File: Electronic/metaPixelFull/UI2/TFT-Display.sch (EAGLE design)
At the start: 34 parts, among them IC1 74HCT14N, IC2 74HCT14N, IC3 74HCT74N, Q1 2N3906

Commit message: minor changes
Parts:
- U$1: value 2.2_TFT_LCD -> 2.2_TFT_LCDNEW; device 2.2"tft:2.2_TFT_LCD -> 2.2"tft:2.2_TFT_LCDNEW
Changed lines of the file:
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@@
 <grid distance="0.1" unitdist="inch" unit="inch" style="lines" multiple="1" display="no" altdistance="0.01" altunitdist="inch" altunit="inch"/>
 <layers>
-<layer number="1" name="Top" color="4" fill="1" visible="no" active="no"/>
-<layer number="2" name="Route2" color="1" fill="3" visible="no" active="no"/>
-<layer number="3" name="Route3" color="4" fill="3" visible="no" active="no"/>
-<layer number="14" name="Route14" color="1" fill="6" visible="no" active="no"/>
-<layer number="15" name="Route15" color="4" fill="6" visible="no" active="no"/>
-<layer number="16" name="Bottom" color="1" fill="1" visible="no" active="no"/>
-<layer number="17" name="Pads" color="2" fill="1" visible="no" active="no"/>
-<layer number="18" name="Vias" color="2" fill="1" visible="no" active="no"/>
-<layer number="19" name="Unrouted" color="6" fill="1" visible="no" active="no"/>
-<layer number="20" name="Dimension" color="15" fill="1" visible="no" active="no"/>
-<layer number="21" name="tPlace" color="7" fill="1" visible="no" active="no"/>
-<layer number="22" name="bPlace" color="7" fill="1" visible="no" active="no"/>
-<layer number="23" name="tOrigins" color="15" fill="1" visible="no" active="no"/>
-<layer number="24" name="bOrigins" color="15" fill="1" visible="no" active="no"/>
-<layer number="25" name="tNames" color="7" fill="1" visible="no" active="no"/>
-<layer number="26" name="bNames" color="7" fill="1" visible="no" active="no"/>
-<layer number="27" name="tValues" color="7" fill="1" visible="no" active="no"/>
-<layer number="28" name="bValues" color="7" fill="1" visible="no" active="no"/>
+<layer number="1" name="Top" color="4" fill="1" visible="yes" active="no"/>
+<layer number="2" name="Route2" color="1" fill="3" visible="yes" active="no"/>
+<layer number="3" name="Route3" color="4" fill="3" visible="yes" active="no"/>
+<layer number="14" name="Route14" color="1" fill="6" visible="yes" active="no"/>
+<layer number="15" name="Route15" color="4" fill="6" visible="yes" active="no"/>
+<layer number="16" name="Bottom" color="1" fill="1" visible="yes" active="no"/>
+<layer number="17" name="Pads" color="2" fill="1" visible="yes" active="no"/>
+<layer number="18" name="Vias" color="2" fill="1" visible="yes" active="no"/>
+<layer number="19" name="Unrouted" color="6" fill="1" visible="yes" active="no"/>
+<layer number="20" name="Dimension" color="15" fill="1" visible="yes" active="no"/>
+<layer number="21" name="tPlace" color="7" fill="1" visible="yes" active="no"/>
+<layer number="22" name="bPlace" color="7" fill="1" visible="yes" active="no"/>
+<layer number="23" name="tOrigins" color="15" fill="1" visible="yes" active="no"/>
+<layer number="24" name="bOrigins" color="15" fill="1" visible="yes" active="no"/>
+<layer number="25" name="tNames" color="7" fill="1" visible="yes" active="no"/>
+<layer number="26" name="bNames" color="7" fill="1" visible="yes" active="no"/>
+<layer number="27" name="tValues" color="7" fill="1" visible="yes" active="no"/>
+<layer number="28" name="bValues" color="7" fill="1" visible="yes" active="no"/>
 <layer number="29" name="tStop" color="7" fill="3" visible="no" active="no"/>
 <layer number="30" name="bStop" color="7" fill="6" visible="no" active="no"/>
@@
 <layer number="35" name="tGlue" color="7" fill="4" visible="no" active="no"/>
 <layer number="36" name="bGlue" color="7" fill="5" visible="no" active="no"/>
-<layer number="37" name="tTest" color="7" fill="1" visible="no" active="no"/>
-<layer number="38" name="bTest" color="7" fill="1" visible="no" active="no"/>
+<layer number="37" name="tTest" color="7" fill="1" visible="yes" active="no"/>
+<layer number="38" name="bTest" color="7" fill="1" visible="yes" active="no"/>
 <layer number="39" name="tKeepout" color="4" fill="11" visible="no" active="no"/>
 <layer number="40" name="bKeepout" color="1" fill="11" visible="no" active="no"/>
@@
 <layer number="44" name="Drills" color="7" fill="1" visible="no" active="no"/>
 <layer number="45" name="Holes" color="7" fill="1" visible="no" active="no"/>
-<layer number="46" name="Milling" color="3" fill="1" visible="no" active="no"/>
-<layer number="47" name="Measures" color="7" fill="1" visible="no" active="no"/>
-<layer number="48" name="Document" color="7" fill="1" visible="no" active="no"/>
-<layer number="49" name="Reference" color="7" fill="1" visible="no" active="no"/>
-<layer number="50" name="dxf" color="7" fill="1" visible="no" active="no"/>
-<layer number="51" name="tDocu" color="7" fill="1" visible="no" active="no"/>
-<layer number="52" name="bDocu" color="7" fill="1" visible="no" active="no"/>
-<layer number="53" name="tGND_GNDA" color="7" fill="9" visible="no" active="no"/>
-<layer number="54" name="bGND_GNDA" color="1" fill="9" visible="no" active="no"/>
-<layer number="56" name="wert" color="7" fill="1" visible="no" active="no"/>
+<layer number="46" name="Milling" color="3" fill="1" visible="yes" active="no"/>
+<layer number="47" name="Measures" color="7" fill="1" visible="yes" active="no"/>
+<layer number="48" name="Document" color="7" fill="1" visible="yes" active="no"/>
+<layer number="49" name="Reference" color="7" fill="1" visible="yes" active="no"/>
+<layer number="50" name="dxf" color="7" fill="1" visible="yes" active="no"/>
+<layer number="51" name="tDocu" color="7" fill="1" visible="yes" active="no"/>
+<layer number="52" name="bDocu" color="7" fill="1" visible="yes" active="no"/>
+<layer number="53" name="tGND_GNDA" color="7" fill="9" visible="yes" active="no"/>
+<layer number="54" name="bGND_GNDA" color="1" fill="9" visible="yes" active="no"/>
+<layer number="56" name="wert" color="7" fill="1" visible="yes" active="no"/>
 <layer number="90" name="Modules" color="5" fill="1" visible="yes" active="yes"/>
 <layer number="91" name="Nets" color="2" fill="1" visible="yes" active="yes"/>
@@
 <part name="FRAME1" library="frames" deviceset="A4L-LOC" device=""/>
 <part name="FRAME2" library="frames" deviceset="A4L-LOC" device=""/>
-<part name="U$1" library="2.2&quot;tft" deviceset="2.2_TFT_LCD" device=""/>
+<part name="U$1" library="2.2&quot;tft" deviceset="2.2_TFT_LCD" device="NEW" value="2.2_TFT_LCDNEW"/>
 <part name="C9" library="rcl" deviceset="C-EU" device="025-024X044" value=".1µ"/>
 <part name="R14" library="resistor" deviceset="R-EU_" device="0204/7" value="15k"/>

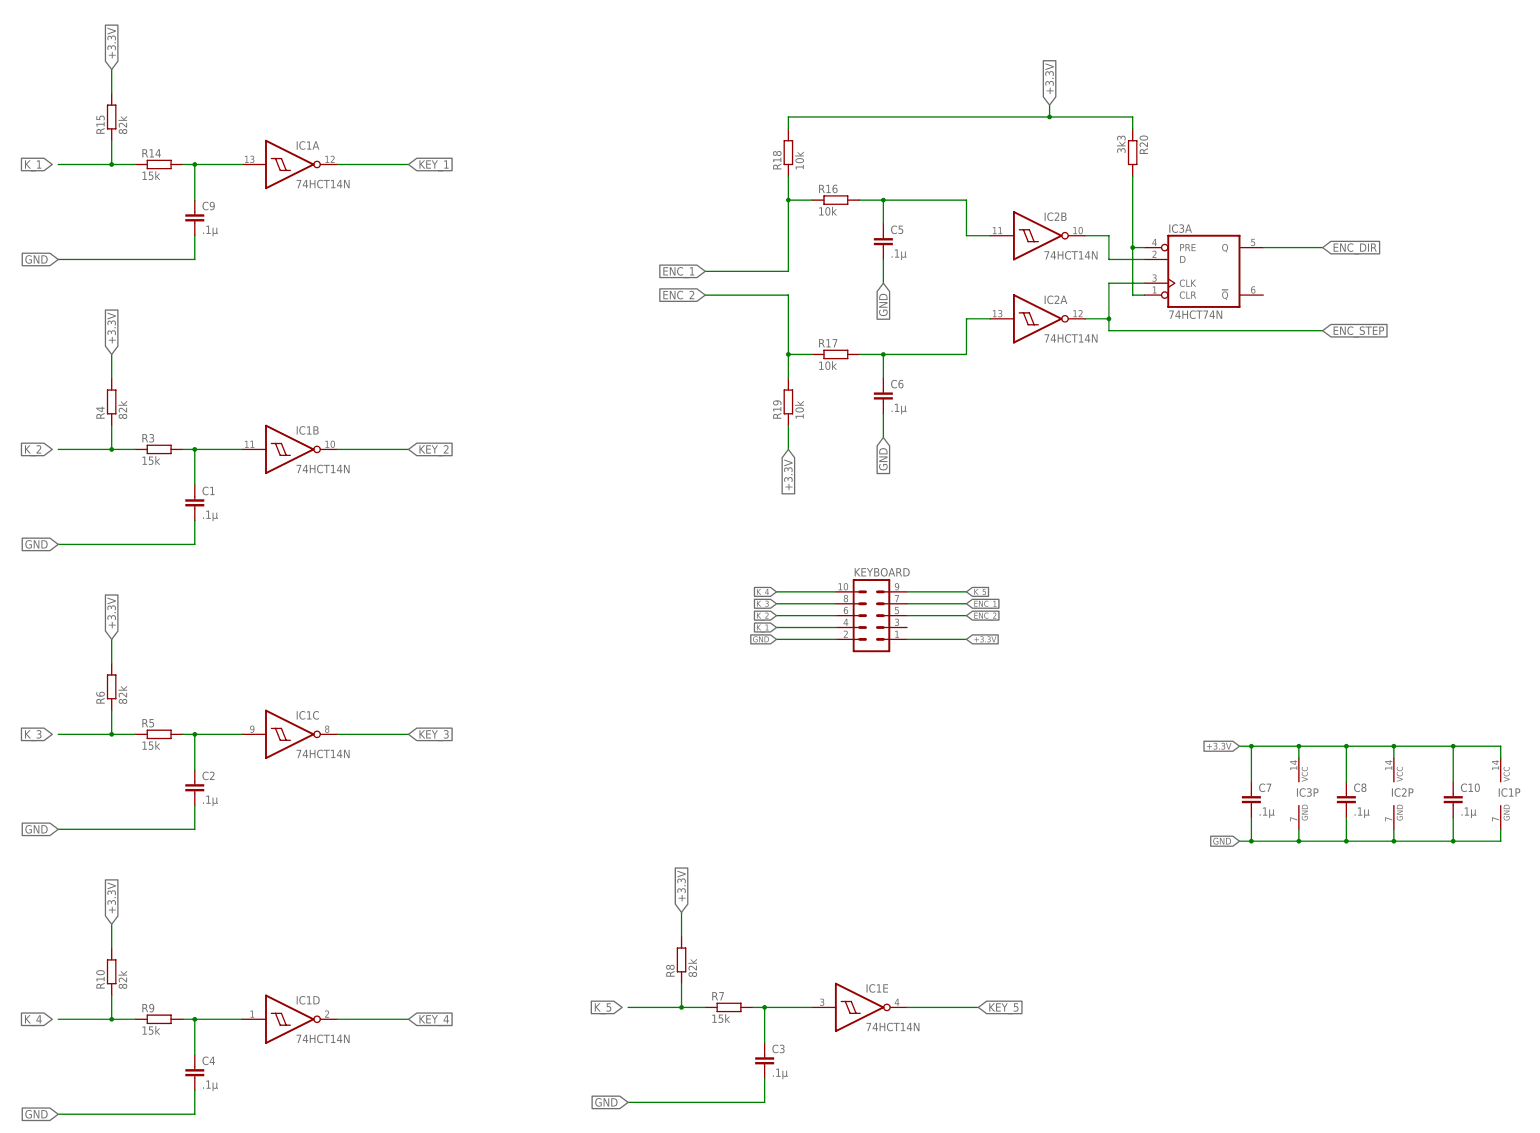
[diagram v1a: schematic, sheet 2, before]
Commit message: Reworking the Controller
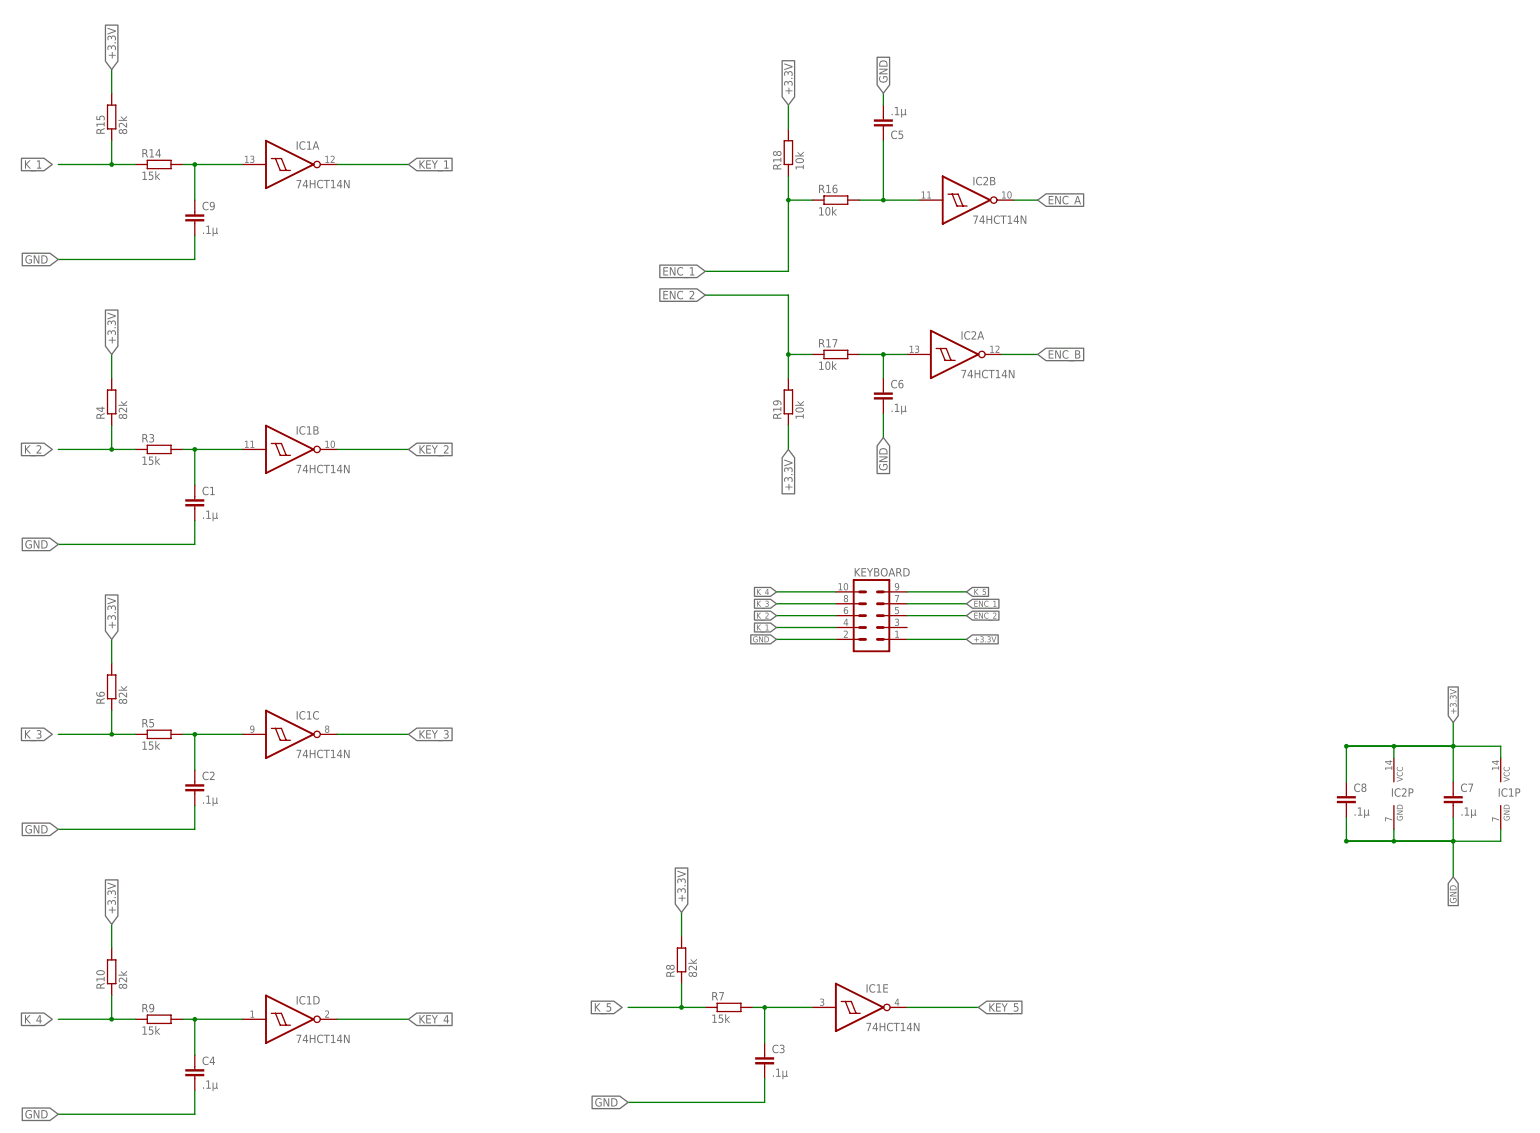
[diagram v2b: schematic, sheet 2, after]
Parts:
- removed C10: .1µ, rcl:C-EU025-024X044
- removed IC3: 74HCT74N, 74xx-eu:74HCT74N
- removed R20: 3k3, resistor:R-EU_0204/7
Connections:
- removed net ENC_DIR: HOST.20, IC3A.Q
- removed net ENC_STEP: HOST.19, IC2A.O, IC3A.CLK
- removed net N$1: IC2B.O, IC3A.D
- removed net N$3: IC3A.CLR, IC3A.PRE, R20.2
- new net ENC_A: HOST.19, IC2B.O
- new net ENC_B: HOST.20, IC2A.O
- net +3.3V: no longer C10.1, IC3P.VCC, R20.1
- net GND: no longer C10.2, IC3P.GND
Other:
- moved on the sheet: C5, C7, IC2A, IC2B
